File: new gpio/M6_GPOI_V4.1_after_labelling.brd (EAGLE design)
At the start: 102.3 x 70.9 mm, 36 parts, among them IC4 LT1161, Q5 16MHz, Q8 16MHz, U3 MCP2515, U4 ATMEGA328P_PDIP, X2 MABC96R

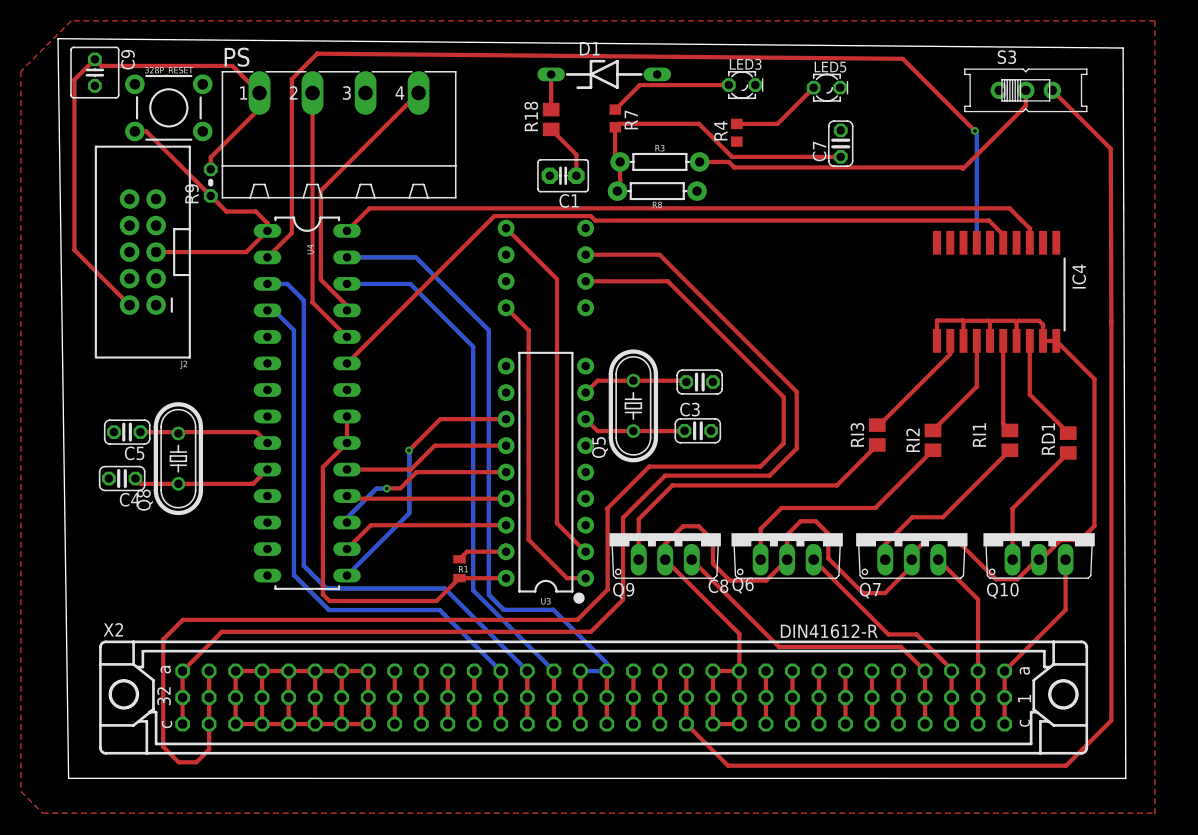
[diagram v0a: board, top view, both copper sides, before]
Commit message: updated with dimensions
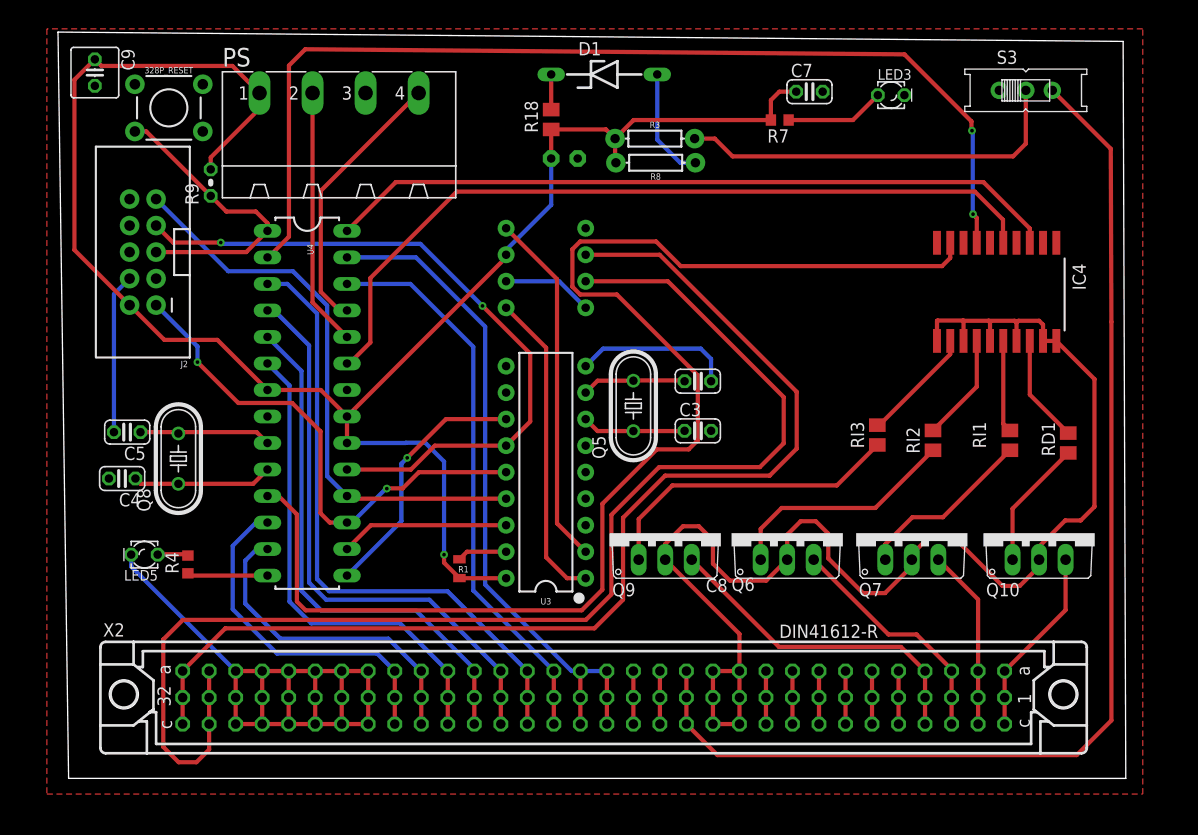
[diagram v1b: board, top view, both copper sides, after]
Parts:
- moved LED5 79.2 mm to (5.23, 20.0), turned to 180 degrees
- moved R4 66.9 mm to (9.40, 19.1)
- moved R7 15.7 mm to (66.1, 61.7), turned to 180 degrees
- moved LED3 14.3 mm to (76.8, 64.1)
- moved C7 5.81 mm to (68.9, 64.4), turned to 0 degrees
- moved R8 2.72 mm to (54.2, 57.6)
- moved R3 2.29 mm to (54.1, 59.9)
- moved C1 1.66 mm to (45.5, 58.0), flipped to the bottom
- moved C8 0.19 mm to (58.2, 36.7)
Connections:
- removed net GND: IC4.1, IC4.10, PS.3
- net DGND: now also IC4.1, IC4.10, PS.3
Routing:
- net PNEU_4_IN: track 0.00 -> 126.8 mm
- net DGND: track 61.1 -> 126.5 mm
- net CAN_SCK: track 16.2 -> 66.9 mm, vias 0 -> 2
- net GPIO_5V: track 124.5 -> 171.8 mm, vias 0 -> 1
- net PWM4: track 5.08 -> 50.6 mm
- net PWM3: track 5.08 -> 46.7 mm
- net CAN_MISO: track 15.3 -> 55.0 mm
- net CAN_MOSI: track 17.5 -> 49.6 mm, vias 1 -> 2
- net PWM1: track 5.08 -> 33.4 mm
- net PWM2: track 5.08 -> 31.3 mm
- net CAN_STAT_1: track 0.00 -> 7.71 mm
- net N$1: track 8.80 -> 2.96 mm
- net PNEU_2_IN: track 71.0 -> 76.7 mm
- net PWM8: track 69.3 -> 65.9 mm
- net GPIO_POWER: track 35.5 -> 38.0 mm
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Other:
- board size 102.3 x 70.9 mm -> 102.3 x 71.5 mm

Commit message: gpio with nobi's changes
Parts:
- removed C1: (no value), capacitor-wima:C2.5-3
- removed D1: 5v, diode:ZDIO-10
- removed LED3, LED5: (no value), eagle-ltspice:LED_LD260
- removed PS: MSTBA4, con-phoenix-508:MSTBA4
- removed R18: (no value), rcl:M0805
- removed R3: 2.2k, SparkFun-Resistors:AXIAL-0.3
- removed R8: 0.732k, SparkFun-Resistors:AXIAL-0.3
- added CAN_STATUS, GPIO_5V: (no value), eagle-ltspice:LED_LD260
- added SL1: (no value), con-amp-quick:03P
- moved U$3 50.4 mm to (4.62, 15.6)
- moved C5 49.2 mm to (52.8, 32.0), turned to 0 degrees
- moved C8 48.6 mm to (15.1, 14.1)
- moved C3 43.4 mm to (15.1, 27.4)
- moved R4 42.2 mm to (45.8, 40.5), turned to 0 degrees
- moved Q5 40.5 mm to (13.9, 20.6), turned to 270 degrees
- moved S3 37.5 mm to (94.5, 27.3), turned to 270 degrees
- moved Q8 34.8 mm to (43.1, 31.9), turned to 0 degrees
- moved C9 32.8 mm to (13.1, 35.9)
- moved C4 31.5 mm to (34.2, 32.1)
- moved U4 30.4 mm to (48.1, 21.1), turned to 180 degrees
- moved C7 28.6 mm to (62.1, 36.7)
- moved R1 27.7 mm to (59.7, 32.1), turned to 180 degrees
- moved R7 20.7 mm to (61.4, 41.5), turned to 0 degrees
- moved U3 20.5 mm to (23.2, 27.0), turned to 270 degrees
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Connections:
- net CRY1 renamed CRY_N
- net CRY2 renamed CRY_P
- net N$10 renamed C_N
- net N$9 renamed C_P
- removed net BUFFER: PS.4, U4.25
- removed net GPIO_5V: C1.1, C7.1, C9.1, J2.2, PS.1, R1.1, R18.1, R3.P$1, R7.2, R8.P$2, R9.2, U$3.3, U3.18, U4.20, U4.21, U4.7
- removed net N$21: D1.C, R18.2
- net DGND: now also CAN_STATUS.K, GPIO_5V.K, SL1.2; no longer C1.2, D1.A, J2.4, J2.6, J2.8, LED3.K, LED5.K, PS.3, R8.P$1
- net GPIO_POWER: now also C7.1, C9.1, J2.2, R1.1, R7.2, R9.2, SL1.3, U$3.3, U3.18, U4.20, U4.21, U4.7; no longer R3.P$2
- net INT_1: now also U4.25
- net N$1: now also CAN_STATUS.A; no longer LED5.A
- net N$4: now also GPIO_5V.A; no longer LED3.A
- net PS_1: now also SL1.1; no longer PS.2
- net PWM1: now also U4.13; no longer U4.12
- net PWM2: now also U4.12; no longer U4.13
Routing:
- net GPIO_5V: track 171.8 -> 0.00 mm, vias 1 -> 0
- net GPIO_POWER: track 38.0 -> 191.5 mm
- net DGND: track 126.5 -> 0.00 mm
- net CAN1_P: track 123.0 -> 18.8 mm
- net CAN1_N: track 108.4 -> 20.2 mm
- net PNEU_4_IN: track 126.8 -> 48.4 mm, vias 0 -> 1
- net PNEU_3_IN: track 99.8 -> 26.5 mm, vias 2 -> 0
- net RESET: track 28.6 -> 86.2 mm
- net GPIO_POWER_IP: track 111.1 -> 57.4 mm
- net PS_1: track 24.7 -> 71.9 mm, vias 0 -> 1
- net PNEU_2_IN: track 76.7 -> 42.5 mm, vias 0 -> 1
- net PNEU_1_IN: track 70.6 -> 37.3 mm
- net N$8: track 4.77 -> 35.4 mm
- net PWM7: track 53.9 -> 24.2 mm
- net PWM8: track 65.9 -> 36.4 mm
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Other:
- board size 102.3 x 71.5 mm -> 101 x 54.6 mm
- board text added: "10u"
- board text added: "5V"
- board text added: "CAN_H"
- board text added: "CAN_L"
- board text added: "DGND"
- board text added: "GPIO_POWER"
- board text added: "INTERRUPTS"
- board text added: "PNEUMATICS"
- board text added: "PS_OUT"
- board text added: "PWM"
- board text added: "pneu_power"

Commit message: FINAL BY LK WITHOUT LABELLING
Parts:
- removed C7: 10u, resistor:C025-024X044
- removed CAN_STATUS, GPIO_5V: (no value), eagle-ltspice:LED_LD260
- removed R1: 10K, SparkFun-Resistors:0805
- removed R4, R7: 0.2k, adafruit:R0603
- removed R9: 10K, rcl:0204V
- added C1, C2: 10u, adafruit:C025-050X050
- added PWR, PWR1: (no value), led:LED5MM
- added R2, R24: 1k, rcl:M0805
- added RD2, RD3: 10K, rcl:M0805
- moved J2 92.1 mm to (94.0, 47.0), turned to 0 degrees
- moved S3 90.9 mm to (3.81, 33.0)
- moved U$3 86.9 mm to (91.4, 20.3), flipped to the top, turned to 270 degrees
- moved C9 79.7 mm to (92.7, 34.3), turned to 0 degrees
- moved Q10 78.7 mm to (12.7, 19.1)
- moved Q7 67.8 mm to (17.8, 19.1)
- moved C3 65.4 mm to (75.4, 52.6)
- moved Q5 62.2 mm to (67.3, 52.6), turned to 180 degrees
- moved C8 58.5 mm to (59.2, 52.6), turned to 180 degrees
- moved Q6 56.9 mm to (22.9, 19.1)
- moved RD1 55.7 mm to (31.5, 27.1)
- moved RI1 55.4 mm to (26.3, 27.1)
- moved RI2 55.0 mm to (21.2, 27.1)
- moved RI3 54.6 mm to (17.0, 27.1)
- moved U3 53.4 mm to (73.7, 44.5), turned to 180 degrees
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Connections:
- removed net N$4: GPIO_5V.A, R7.1
- new net N$31: PWR.A, R24.1
- net CAN_STAT_1: now also R2.2; no longer R4.1
- net DGND: now also C1.2, C2.2, PWR.K, PWR1.K; no longer C7.2, CAN_STATUS.K, GPIO_5V.K
- net GPIO_POWER: now also C1.1, C2.1, R24.2, RD2.2, RD3.1; no longer C7.1, R1.1, R7.2, R9.2
- net N$1: now also PWR1.A, R2.1; no longer CAN_STATUS.A, R4.2
- net N$8: now also RD2.1; no longer R1.2
- net PNEU_1_IN: now also IC4.9, U4.24; no longer IC4.3, U4.28
- net PNEU_1_OUT: now also RI3.1; no longer RD1.1
- net PNEU_2_IN: now also IC4.7, U4.26; no longer IC4.5, U4.23
- net PNEU_2_OUT: now also RI2.1; no longer RI1.1
- net PNEU_3_IN: now also IC4.5, U4.27; no longer IC4.7, U4.2
- net PNEU_3_OUT: now also RI1.1; no longer RI2.1
- net PNEU_4_IN: now also IC4.3, U4.28; no longer IC4.9, U4.11
- net PNEU_4_OUT: now also RD1.1; no longer RI3.1
- net PS_1: now also U4.23; no longer U4.24
- net PWM3: now also U4.11; no longer U4.6
- net PWM4: now also U4.6; no longer U4.5
- net PWM5: now also U4.5; no longer U4.4
- net PWM6: now also U4.4; no longer U4.3
- net PWM7: now also U4.3; no longer U4.26
- net PWM8: now also U4.2; no longer U4.27
- net RESET: now also RD3.2; no longer R9.1
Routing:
- net RESET: track 86.2 -> 172.1 mm, vias 0 -> 1
- net DGND: track 0.00 -> 68.6 mm
- net PS_1: track 71.9 -> 21.8 mm, vias 1 -> 0
- net CAN_SCK: track 62.9 -> 29.7 mm, vias 0 -> 1
- net CAN_MISO: track 55.9 -> 23.3 mm
- net CAN_STAT_1: track 25.6 -> 56.9 mm, vias 1 -> 0
- net CAN_SS: track 32.6 -> 5.08 mm, vias 2 -> 0
- net PNEU_4_IN: track 48.4 -> 23.2 mm, vias 1 -> 0
- net N$8: track 35.4 -> 10.5 mm
- net INT_1: track 25.7 -> 47.6 mm, vias 1 -> 0
- net GPIO_POWER: track 191.5 -> 210.5 mm, vias 0 -> 1
- net CAN_INT: track 15.2 -> 32.1 mm, vias 1 -> 0
- net GPIO_POWER_IP: track 57.4 -> 71.5 mm
- net PWM4: track 37.1 -> 24.6 mm
- net N$7: track 24.9 -> 37.2 mm
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- added copper zone on layer 16, net DGND
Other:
- board size 101 x 54.6 mm -> 100 x 58.4 mm
- board text removed: "10u"
- board text removed: "5V"
- board text removed: "CAN_H"
- board text removed: "CAN_L"
- board text removed: "DGND"
- board text removed: "GPIO_POWER"
- board text removed: "INTERRUPTS"
- board text removed: "PNEUMATICS"
- board text removed: "PS_OUT"
- board text removed: "PWM"
- board text removed: "pneu_power"
